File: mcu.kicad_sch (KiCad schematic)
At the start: 202 parts, among them IC1 SKY13373-460LF, IC10 TPS22965NTDSGRQ1, IC2 AD8318ACPZ-REEL7, IC3 AD8318ACPZ-REEL7, IC4 TPS2121RUXT, IC5 MAX17048G+T10, IC6 MAX17048G+T10, IC7 TCA9543ADR, IC8 MAX16150AUT+T, IC9 SN74LVC1G74RSE2, J1 Interface, J3 Board_1, J4 JST_MAIN, M1 Motor_DC, Q1 AO3400A, Q2 AO3400A, Q3 AO3400A, Q4 AO3401A, SW1 POWER, U1 ESP32-S3-WROOM-2, U10 DRV2605LDGS, U11 LC76G, U12 RV-3028-C7, U13 SA818S, U14 INA219BxDCN, U15 INA219BxDCN, U16 INA219BxDCN, U17 MCP4725xxx-xCH, U18 TLV3501AIDBV, U2 TCD-10-23BDX+, U21 WM8960, U23 E22-900M30S, U24 E22-170M30S, U3 MCP23017x-x-ML, U4 BMP390, U5 IS31FL3218-QF, U6 LSM6DSOXTR, U7 BQ24075RGT, U8 MCP23017x-x-ML, U9 BQ24075RGT

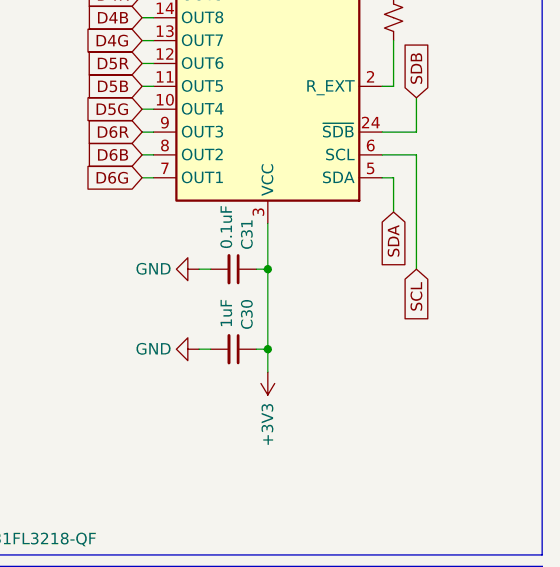
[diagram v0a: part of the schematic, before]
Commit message: Routed power section in the layout
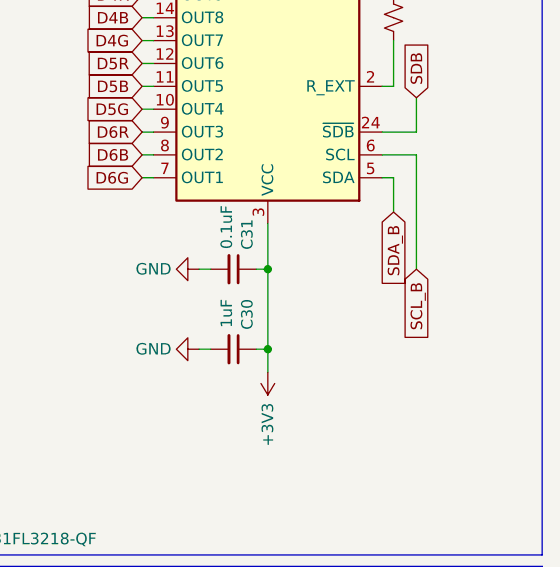
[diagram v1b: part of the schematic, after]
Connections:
- net SCL: no longer U5.6 (SCL)
- net SDA: no longer U5.5 (SDA)
- new net SCL_B: U5.6 (SCL)
- new net SDA_B: U5.5 (SDA)
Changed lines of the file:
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@@
 		)
 	)
-	(global_label "SDA"
+	(global_label "SDA_B"
 		(shape input)
 		(at 563.88 87.63 270)
@@
 		)
 		(property "Intersheetrefs" "${INTERSHEET_REFS}"
-			(at 563.88 94.1833 90)
+			(at 563.88 96.4209 90)
 			(hide yes)
 			(show_name no)
@@
 		)
 	)
-	(global_label "SCL"
+	(global_label "SCL_B"
 		(shape input)
 		(at 566.42 93.98 270)
@@
 		)
 		(property "Intersheetrefs" "${INTERSHEET_REFS}"
-			(at 566.42 100.4728 90)
-			(hide yes)
-			(show_name no)
+			(at 566.42 102.7104 90)
+			(hide yes)
+			(show_name no)

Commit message: Finished routing main PCB
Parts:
- removed C129: 2.2uF, Capacitor_SMD:C_0402_1005Metric, symbol Device:C_Small
- removed C91, C92: 100nF, Capacitor_SMD:C_0402_1005Metric, symbol Device:C_Small
- added C135, C137: 100nF, Capacitor_SMD:C_0402_1005Metric, symbol Device:C_Small
- added C136: 22uF, Capacitor_SMD:C_0402_1005Metric, symbol Device:C_Small
- added R141: 3.3K, Resistor_SMD:R_0402_1005Metric, symbol Device:R_Small_US
- M1: footprint Connector_PinHeader_1.27mm:PinHeader_1x02_P1.27mm_Vertical -> Connector_Molex:Molex_PicoBlade_53048-0210_1x02_P1.25mm_Horizontal
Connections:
- net +3V3: now also C137.1
- net +3V3_RADIO_OUT: now also C135.1
- net +5V: no longer C118.2, C98.2, U7.13 (IN), U9.13 (IN)
- net BAT1: now also C98.2, U7.13 (IN)
- net BAT2: now also C118.2, U9.13 (IN)
- net GND: now also C135.2, C136.2, C137.2, R141.2
- net MOTOR: now also U8.3 (GPB6); no longer U3.1 (GPB4)
- net SDB_1: now also U3.25 (GPB0); no longer U3.19 (GPA2)
- net VIN: now also C136.1, R141.1
- net AUDIO_ON: no longer names the net of U13.1 (AUDIO_ON)
- no-connect marks 33 -> 36
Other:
- moved on the sheet: R98

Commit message: Routed all PCB, missing antenna variable capacitors
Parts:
- removed AE1: GNSS, Connector_Coaxial:U.FL_Molex_MCRF_73412-0110_Vertical, symbol Device:Antenna_Shield
- removed C10, C14: 100pF, Capacitor_SMD:C_0402_1005Metric, symbol Device:C_Small
- removed C11, C12: NC, Capacitor_SMD:C_0402_1005Metric, symbol Device:C_Small
- removed C13, C6: 100nF, Capacitor_SMD:C_0402_1005Metric, symbol Device:C_Small
- removed C7: 10uF, Capacitor_SMD:C_0402_1005Metric, symbol Device:C_Small
- removed D7: D_TVS, Diode_SMD:D_SOD-923, symbol Device:D_TVS
- removed J3: Board_1, Connector_FFC-FPC:Molex_502244-3330_1x33-1MP_P0.5mm_Horizontal, symbol Connector_Generic:Conn_02x16_Counter_Clockwise
- removed L2: 68nH, Inductor_SMD:L_0402_1005Metric, symbol Device:L
- removed R125: 0R, Resistor_SMD:R_0402_1005Metric, symbol Device:R_Small_US
- removed R126: 10R, Resistor_SMD:R_0402_1005Metric, symbol Device:R_Small_US
- removed R99: 10K, Resistor_SMD:R_0402_1005Metric, symbol Device:R_Small_US
- removed U11: LC76G, PTCR:XCVR_LC76G, symbol PTCR-V5:LC76G
- added J3: L76K, PTCR:JST_SM08B-SRSS-TB_LF__SN_, symbol Connector_Generic:Conn_01x08
- added J6: Board_1, Connector_FFC-FPC:Molex_502244-3330_1x33-1MP_P0.5mm_Horizontal, symbol Connector_Generic:Conn_02x17_Counter_Clockwise
- C122, C124: footprint Capacitor_SMD:C_0603_1608Metric -> Capacitor_SMD:C_0402_1005Metric
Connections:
- net CS_GNSS is gone; now on net GNSS_TX: U1.35 (MTMS/IO42)
- net POWER_BTN_B is gone; now on net POWER_BTN: D8.2 (A), IC8.1 (~{PB_IN}), R129.1, SW1.1
- net +3V3: now also J6.31 (Pin_31), J6.32 (Pin_32), J6.33 (Pin_33)
- net +3V3_GNSS: now also J3.3 (Pin_3)
- net +5V: now also J6.7 (Pin_7), J6.8 (Pin_8), J6.9 (Pin_9)
- net BAT1_CHG_1: now also J6.29 (Pin_29)
- net BAT1_PGOOD_1: now also J6.30 (Pin_30)
- net BAT2_CHG_1: now also J6.27 (Pin_27)
- net BAT2_PGOOD_1: now also J6.28 (Pin_28)
- net BATS_INT_1: now also J6.17 (Pin_17)
- net BATS_RESET_1: now also J6.13 (Pin_13)
- net BAT_SEL_1: now also J6.16 (Pin_16)
- net BAT_VAL_1: now also J6.14 (Pin_14)
- net BUTTON0: now also J6.19 (Pin_19)
- net BUTTON1: now also J6.20 (Pin_20)
- net GND: now also J3.1 (Pin_1), J6.10 (Pin_10), J6.11 (Pin_11), J6.12 (Pin_12), J6.3 (Pin_3), J6.4 (Pin_4), J6.5 (Pin_5), J6.6 (Pin_6)
- net G_RESET: now also J3.8 (Pin_8)
- net JOYSTICK_X: now also J6.22 (Pin_22)
- net JOYSTICK_Y: now also J6.21 (Pin_21)
- net POWER_BTN: now also J6.18 (Pin_18)
- net ROT_ENC1: now also J6.24 (Pin_24)
- net ROT_ENC2: now also J6.23 (Pin_23)
- net SCL: now also J6.25 (Pin_25)
- net SDA: now also J6.26 (Pin_26)
- net SDB_1: now also J6.2 (Pin_2)
- net SHUTDOWN_1: now also J6.15 (Pin_15)
- net GNSS_RX: now reaches TP1.1
- net GNSS_RX: now also U1.34 (MTDI/IO41), J3.5 (Pin_5)
- net GNSS_TX: now reaches TP3.1
- net GNSS_TX: now also J3.4 (Pin_4)
- net GNSS_CTRL: now reaches U3.19 (GPA2)
- net GNSS_CTRL: now also J3.2 (Pin_2)
- net GNSS_WAKE: now reaches U3.24 (GPA7)
- net GNSS_WAKE: now also J3.6 (Pin_6)
- no-connect marks 36 -> 28
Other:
- note removed: "GNSS Antenna"
- moved on the sheet: TP1, TP3

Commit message: Finishing routing unrouted nets and verifying DRC
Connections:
- net +5V: no longer J6.7 (Pin_7), J6.8 (Pin_8), J6.9 (Pin_9)
- net BAT_OUT: now also J6.7 (Pin_7), J6.8 (Pin_8), J6.9 (Pin_9)
- net SCL: no longer IC7.12 (SCL)
- net SCL_B: now also IC7.12 (SCL)
- net SDA: no longer IC7.13 (SDA)
- net SDA_B: now also IC7.13 (SDA)
